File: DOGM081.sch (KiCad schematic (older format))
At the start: 1 part

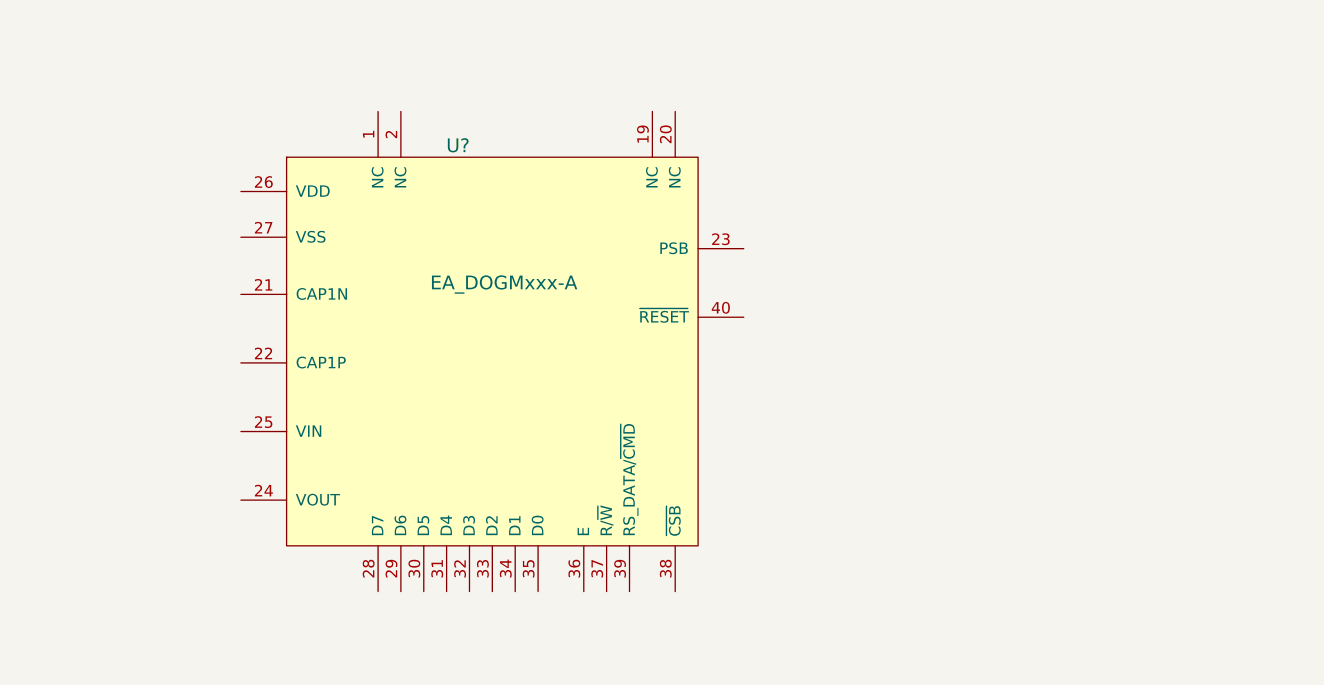
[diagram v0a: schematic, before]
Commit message: Layout completed and sent to OSH Park
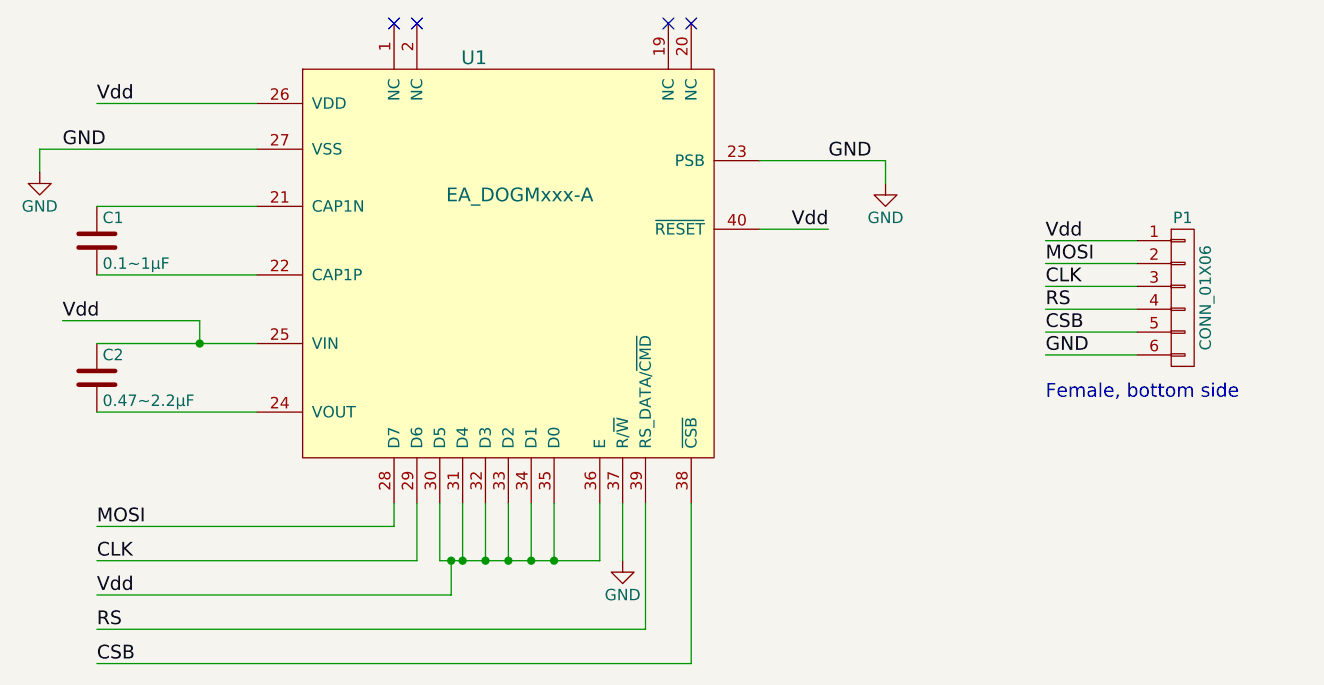
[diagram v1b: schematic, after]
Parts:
- removed U?: EA_DOGMxxx-A, symbol EA_DOGMxxx-A
- added C1: 0.1~~1μF, Capacitors_SMD:C_1206_HandSoldering, symbol C
- added C2: 0.47~~2.2μF, Capacitors_SMD:C_1206_HandSoldering, symbol C
- added P1: CONN_01X06, Socket_Strips:Socket_Strip_Straight_1x06_Pitch2.54mm, symbol CONN_01X06
- added U1: EA_DOGMxxx-A, DisplayAdapter_DOGM081_Symbols:EA_DOGM081x-A, symbol EA_DOGMxxx-A
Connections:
- new net: C1.1, U1.21 (CAP1N)
- new net: C1.2, U1.22 (CAP1P)
- new net: C2.2, U1.24 (VOUT)
- new net CLK: P1.3 (P3), U1.29 (D6)
- new net CSB: P1.5 (P5), U1.38 (~CSB)
- new net GND: P1.6 (P6), U1.23 (PSB), U1.27 (VSS), U1.37 (R/~W)
- new net MOSI: P1.2 (P2), U1.28 (D7)
- new net RS: P1.4 (P4), U1.39 (RS_DATA/~CMD)
- new net Vdd: C2.1, P1.1 (P1), U1.25 (VIN), U1.26 (VDD), U1.30 (D5), U1.31 (D4), U1.32 (D3), U1.33 (D2), U1.34 (D1), U1.35 (D0), U1.36 (E), U1.40 (~RESET)
- no-connect marks 0 -> 4
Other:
- note added: "Female, bottom side"
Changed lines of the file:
@@
 LIBS:contrib
 LIBS:valves
+LIBS:DOGM081-cache
 EELAYER 25 0
 EELAYER END
@@
 Comment4 ""
 $EndDescr
-$Comp
-L EA_DOGMxxx-A U?
-U 1 1 598A1AAE
-P 4480 3285
-F 0 "U?" H 4330 4185 60  0000 C CNN
-F 1 "EA_DOGMxxx-A" H 4530 3585 60  0000 C CNN
-F 2 "" V 3380 5935 60  0000 C CNN
-F 3 "" V 3380 5935 60  0000 C CNN
-	1    4480 3285
-	1    0    0    -1
-$EndComp
+Text Label 2750 2200 0    60   ~ 0
+Vdd
+$Comp
+L EA_DOGMxxx-A U1
+U 1 1 598B1EF0
+P 4550 2900
+F 0 "U1" H 4400 3800 60  0000 C CNN
+F 1 "EA_DOGMxxx-A" H 4600 3200 60  0000 C CNN
+F 2 "DisplayAdapter_DOGM081_Symbols:EA_DOGM081x-A" V 3450 5550 60  0001 C CNN
+F 3 "" V 3450 5550 60  0000 C CNN
+	1    4550 2900
+	1    0    0    -1
+$EndComp
+Text Label 5950 2750 2    60   ~ 0
+Vdd
+$Comp
+L C C1
+U 1 1 598B1F2D
+P 2750 2800
+F 0 "C1" H 2775 2900 50  0000 L CNN
+F 1 "0.1~~1μF" H 2775 2700 50  0000 L CNN
+F 2 "Capacitors_SMD:C_1206_HandSoldering" H 2788 2650 30  0001 C CNN
+F 3 "" H 2750 2800 60  0000 C CNN
+F 4 "Value" H 2750 2800 60  0001 C CNN "Link"
+	1    2750 2800
+	1    0    0    -1
+$EndComp
+$Comp
+L C C2
+U 1 1 598B1FC7
+P 2750 3400
+F 0 "C2" H 2775 3500 50  0000 L CNN
+F 1 "0.47~~2.2μF" H 2775 3300 50  0000 L CNN
+F 2 "Capacitors_SMD:C_1206_HandSoldering" H 2788 3250 30  0001 C CNN
+F 3 "" H 2750 3400 60  0000 C CNN
+F 4 "Value" H 2750 3400 60  0001 C CNN "Link"
+	1    2750 3400
+	1    0    0    -1
+$EndComp
+Wire Wire Line
+	3450 2650 2750 2650
+Wire Wire Line
+	3450 2950 2750 2950
+Wire Wire Line
+	2750 3250 3450 3250
+Wire Wire Line
+	3450 3550 2750 3550
+Wire Wire Line
+	3200 3250 3200 3150
+Wire Wire Line
+	3200 3150 2600 3150
+Connection ~ 3200 3250
+Text Label 2600 3150 0    60   ~ 0
+Vdd
+Wire Wire Line
+	3450 2200 2750 2200
+Wire Wire Line
+	3450 2400 2500 2400
+Wire Wire Line
+	2500 2400 2500 2500
+$Comp
+L GND #PWR01
+U 1 1 598B209F
+P 2500 2500
+F 0 "#PWR01" H 2500 2250 50  0001 C CNN
+F 1 "GND" H 2500 2350 50  0000 C CNN
+F 2 "" H 2500 2500 60  0000 C CNN
+F 3 "" H 2500 2500 60  0000 C CNN
+	1    2500 2500
+	1    0    0    -1
+$EndComp
+Wire Wire Line
+	4050 3950 4050 4050
+Wire Wire Line
+	4050 4050 2750 4050
+Wire Wire Line
+	4150 3950 4150 4200
+Wire Wire Line
+	4150 4200 2750 4200
+Wire Wire Line
+	4250 3950 4250 4200
+Wire Wire Line
+	4250 4200 4950 4200
+Wire Wire Line
+	4950 4200 4950 3950
+Wire Wire Line
+	4350 3950 4350 4200
+Connection ~ 4350 4200
+Wire Wire Line
+	4450 3950 4450 4200
+Connection ~ 4450 4200
+Wire Wire Line
+	4550 3950 4550 4200
+Connection ~ 4550 4200
+Wire Wire Line
+	4650 3950 4650 4200
+Connection ~ 4650 4200
+Wire Wire Line
+	4750 3950 4750 4200
+Connection ~ 4750 4200
+Wire Wire Line
+	4300 4200 4300 4350
+Wire Wire Line
+	4300 4350 2750 4350
+Connection ~ 4300 4200
+Text Label 2750 4350 0    60   ~ 0
+Vdd
+$Comp
+L GND #PWR02
+U 1 1 598B248A
+P 5050 4200
+F 0 "#PWR02" H 5050 3950 50  0001 C CNN
+F 1 "GND" H 5050 4050 50  0000 C CNN
+F 2 "" H 5050 4200 60  0000 C CNN
+F 3 "" H 5050 4200 60  0000 C CNN
+	1    5050 4200
+	1    0    0    -1
+$EndComp
+Wire Wire Line
+	5050 3950 5050 4200
+Wire Wire Line
+	5150 3950 5150 4500
+Wire Wire Line
+	5150 4500 2750 4500
+Wire Wire Line
+	5350 3950 5350 4650
+Wire Wire Line
+	5350 4650 2750 4650
+$Comp
+L GND #PWR03
+U 1 1 598B252B
+P 6200 2550
+F 0 "#PWR03" H 6200 2300 50  0001 C CNN
+F 1 "GND" H 6200 2400 50  0000 C CNN
+F 2 "" H 6200 2550 60  0000 C CNN
+F 3 "" H 6200 2550 60  0000 C CNN
+	1    6200 2550
+	1    0    0    -1
+$EndComp
+Wire Wire Line
+	5650 2750 5950 2750
+Wire Wire Line
+	6200 2550 6200 2450
+Wire Wire Line
+	6200 2450 5650 2450
+NoConn ~ 4050 1850
+NoConn ~ 4150 1850
+NoConn ~ 5250 1850
+NoConn ~ 5350 1850
+Text Label 2750 4050 0    60   ~ 0
+MOSI
+Text Label 2750 4200 0    60   ~ 0
+CLK
+Text Label 2750 4500 0    60   ~ 0
+RS
+Text Label 2750 4650 0    60   ~ 0
+CSB
+$Comp
+L CONN_01X06 P1
+U 1 1 598B27C6
+P 7500 3050
+F 0 "P1" H 7500 3400 50  0000 C CNN
+F 1 "CONN_01X06" V 7600 3050 50  0000 C CNN
+F 2 "Socket_Strips:Socket_Strip_Straight_1x06_Pitch2.54mm" H 7500 3050 60  0001 C CNN
+F 3 "" H 7500 3050 60  0000 C CNN
+	1    7500 3050
+	1    0    0    -1
+$EndComp
+Wire Wire Line
+	7300 2800 6900 2800
+Wire Wire Line
+	7300 2900 6900 2900
+Wire Wire Line
+	7300 3000 6900 3000
+Wire Wire Line
+	7300 3100 6900 3100
+Wire Wire Line
+	7300 3200 6900 3200
+Wire Wire Line
+	7300 3300 6900 3300
+Text Label 2600 2400 0    60   ~ 0
+GND
+Text Label 5950 2450 0    60   ~ 0
+GND
+Text Label 6900 3300 0    60   ~ 0
+GND
+Text Label 6900 2800 0    60   ~ 0
+Vdd
+Text Label 6900 2900 0    60   ~ 0
+MOSI
+Text Label 6900 3000 0    60   ~ 0
+CLK
+Text Label 6900 3100 0    60   ~ 0
+RS
+Text Label 6900 3200 0    60   ~ 0
+CSB
+Text Notes 6900 3500 0    60   ~ 0
+Female, bottom side
 $EndSCHEMATC
